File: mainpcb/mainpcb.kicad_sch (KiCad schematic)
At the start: 0 parts

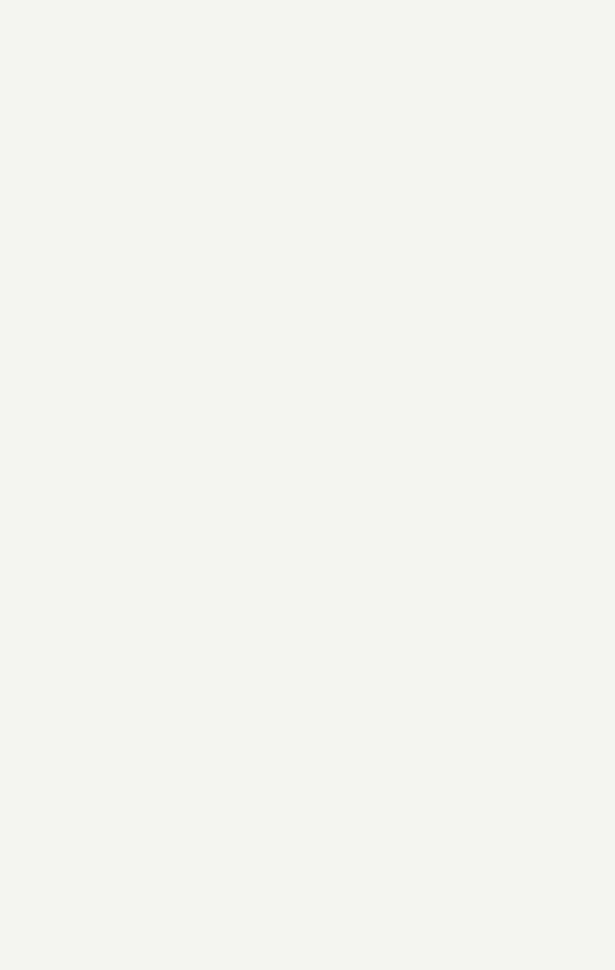
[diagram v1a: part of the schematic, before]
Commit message: Some hand components, PSU changes
Updated PSU to 24V rail regulated to 5V and 3.3V. Hopefully we won't need a 12V rail. Made some part selections, added IO expander for hand, mosfet, made solenoid symbol.
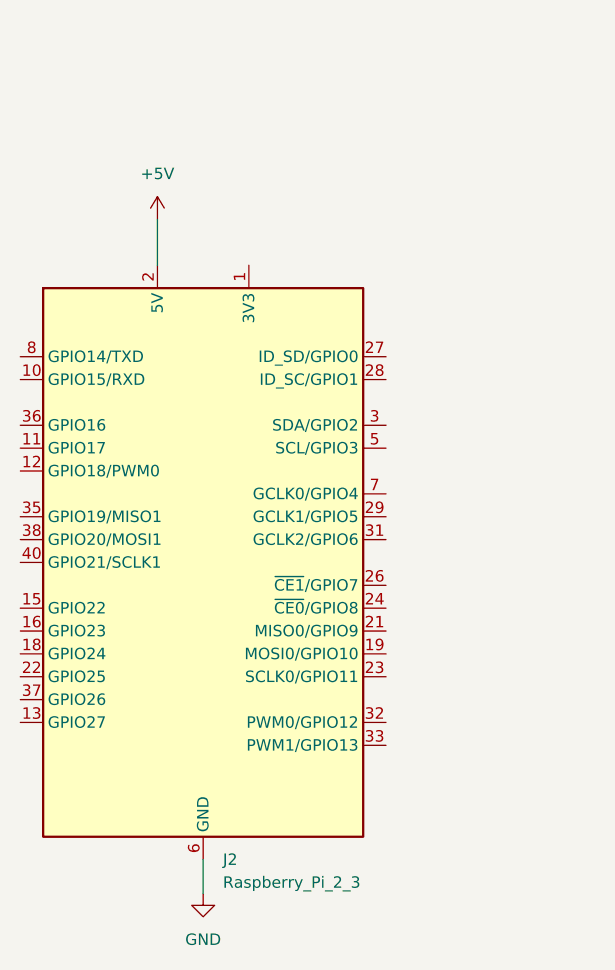
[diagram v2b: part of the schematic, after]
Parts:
- added J2: Raspberry_Pi_2_3, Connector_PinHeader_2.54mm:PinHeader_2x20_P2.54mm_Vertical, symbol Connector:Raspberry_Pi_2_3
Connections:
- new net: J2.1 (3V3), J2.17 (3V3)
- new net +5V: J2.2 (5V), J2.4 (5V)
- new net GND: J2.14 (GND), J2.20 (GND), J2.25 (GND), J2.30 (GND), J2.34 (GND), J2.39 (GND), J2.6 (GND), J2.9 (GND)

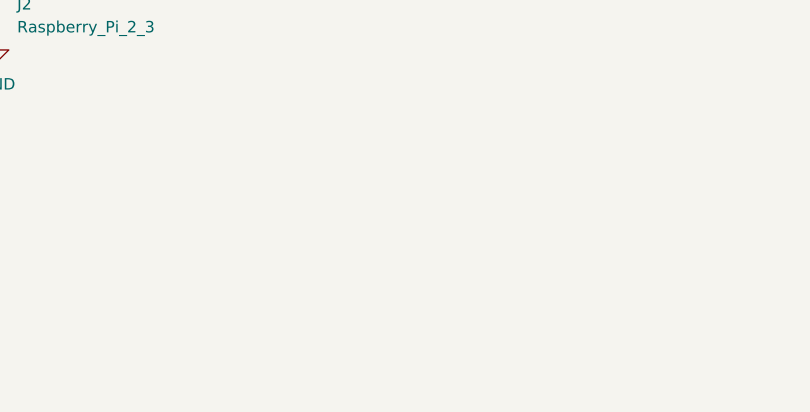
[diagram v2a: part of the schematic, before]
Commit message: Added PCA9615 differential I2C buffer
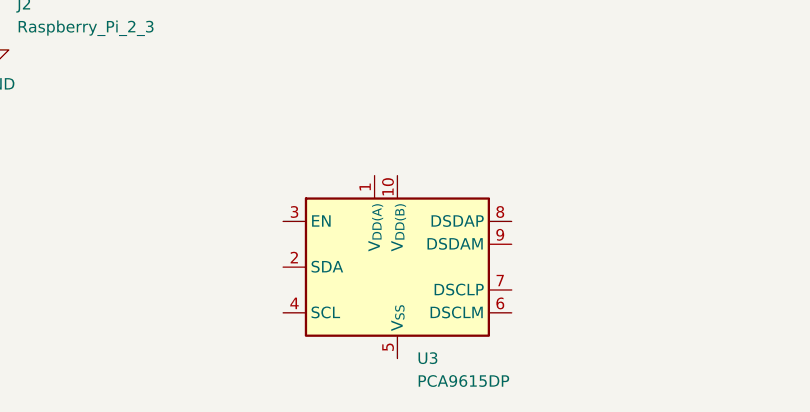
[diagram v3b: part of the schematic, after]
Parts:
- added U3: PCA9615DP, Package_SO:TSSOP-10_3x3mm_P0.5mm, symbol Interface:PCA9615DP
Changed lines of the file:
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@@
+	)
+	(symbol
+		(lib_id "Interface:PCA9615DP")
+		(at 137.16 170.18 0)
+		(unit 1)
+		(exclude_from_sim no)
+		(in_bom yes)
+		(on_board yes)
+		(dnp no)
+		(fields_autoplaced yes)
+		(property "Reference" "U3"
+			(at 139.3541 180.34 0)
+			(effects
+				(font
+					(size 1.27 1.27)
+				)
+				(justify left)
+			)
+		)
+		(property "Value" "PCA9615DP"
+			(at 139.3541 182.88 0)
+			(effects
+				(font
+					(size 1.27 1.27)
+				)
+				(justify left)
+			)
+		)
+		(property "Footprint" "Package_SO:TSSOP-10_3x3mm_P0.5mm"
+			(at 157.48 179.07 0)
+			(effects
+				(font
+					(size 1.27 1.27)
+				)
+				(hide yes)
+			)
+		)
+		(property "Datasheet" "https://www.nxp.com/docs/en/data-sheet/PCA9615.pdf"
+			(at 137.16 181.61 0)
+			(effects
+				(font
+					(size 1.27 1.27)
+				)
+				(hide yes)
+			)
+		)
+		(property "Description" "Dual bidirectional hot-swap multipoint bus buffer, SO-8"
+			(at 137.16 170.18 0)
+			(effects
+				(font
+					(size 1.27 1.27)
+				)
+				(hide yes)
+			)
+		)
+		(property "Digikey" "https://www.digikey.ca/en/products/detail/nxp-usa-inc/PCA9615DPZ/14635231"
+			(at 137.16 170.18 0)
+			(effects
+				(font
+					(size 1.27 1.27)
+				)
+				(hide yes)
+			)
+		)
+		(pin "9"
+		)
+		(pin "2"
+		)
+		(pin "4"
+		)
+		(pin "7"
+		)
+		(pin "10"
+		)
+		(pin "6"
+		)
+		(pin "3"
+		)
+		(pin "5"
+		)
+		(pin "1"
+		)
+		(pin "8"
+		)
+		(instances
+			(project "mainpcb"
+				(path "/8e899647-a0f4-47d2-9d4a-2e9de2221eca"
+					(reference "U3")
+					(unit 1)
+				)
+			)
+		)
 	)
 	(symbol

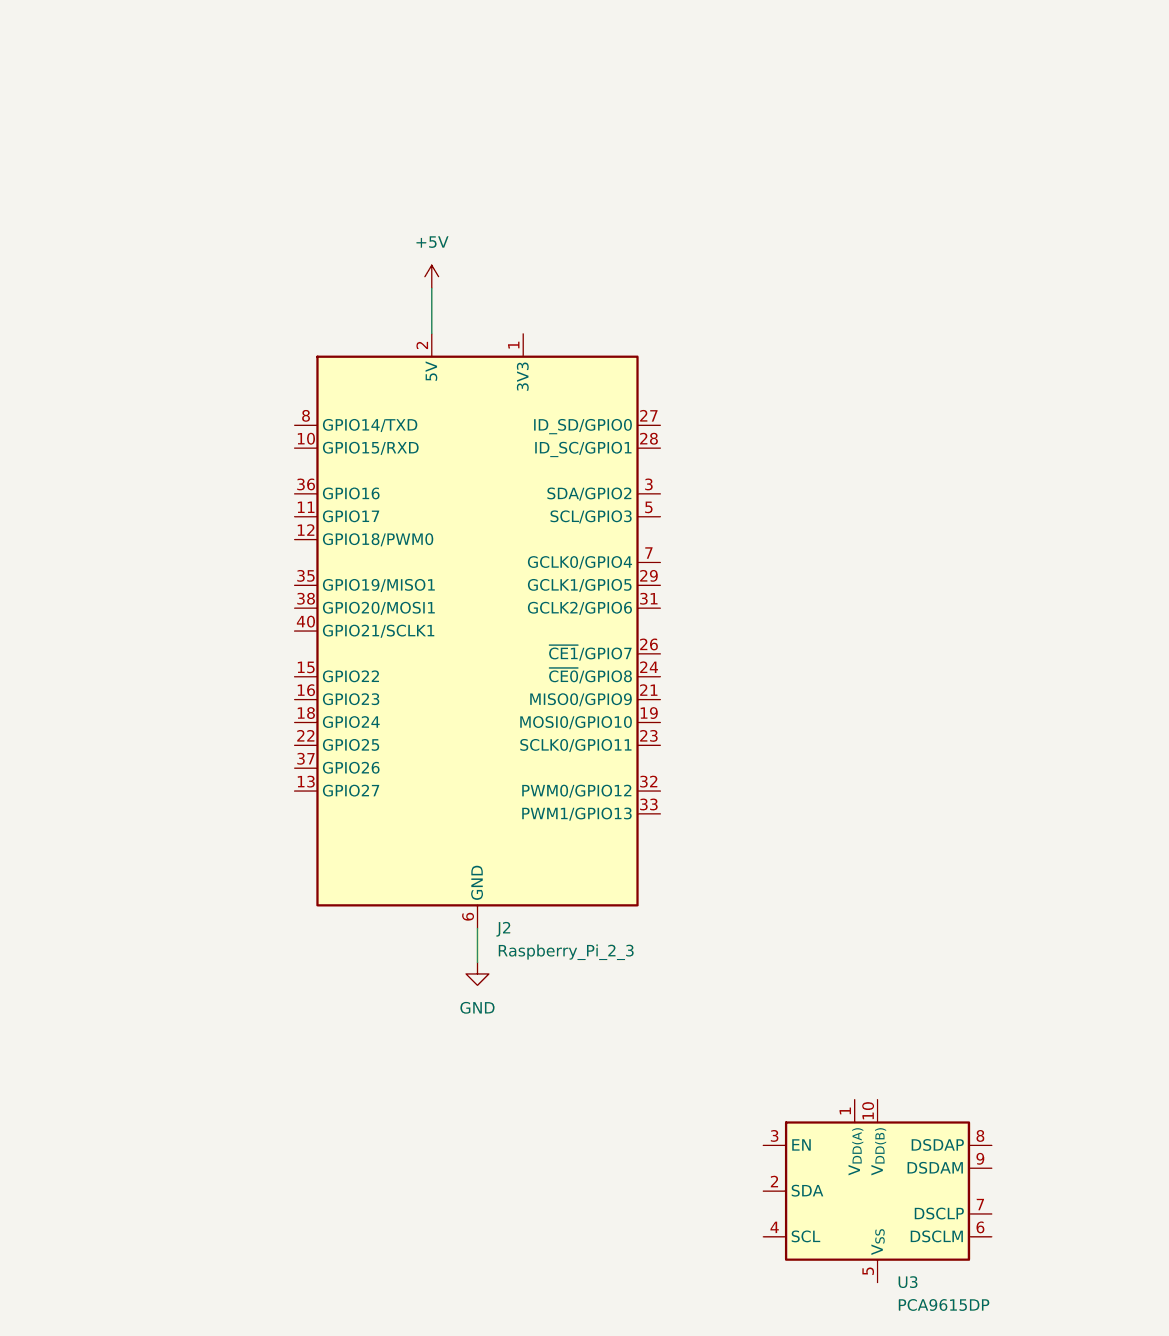
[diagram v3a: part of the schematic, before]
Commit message: Added 12V power rail and regulator
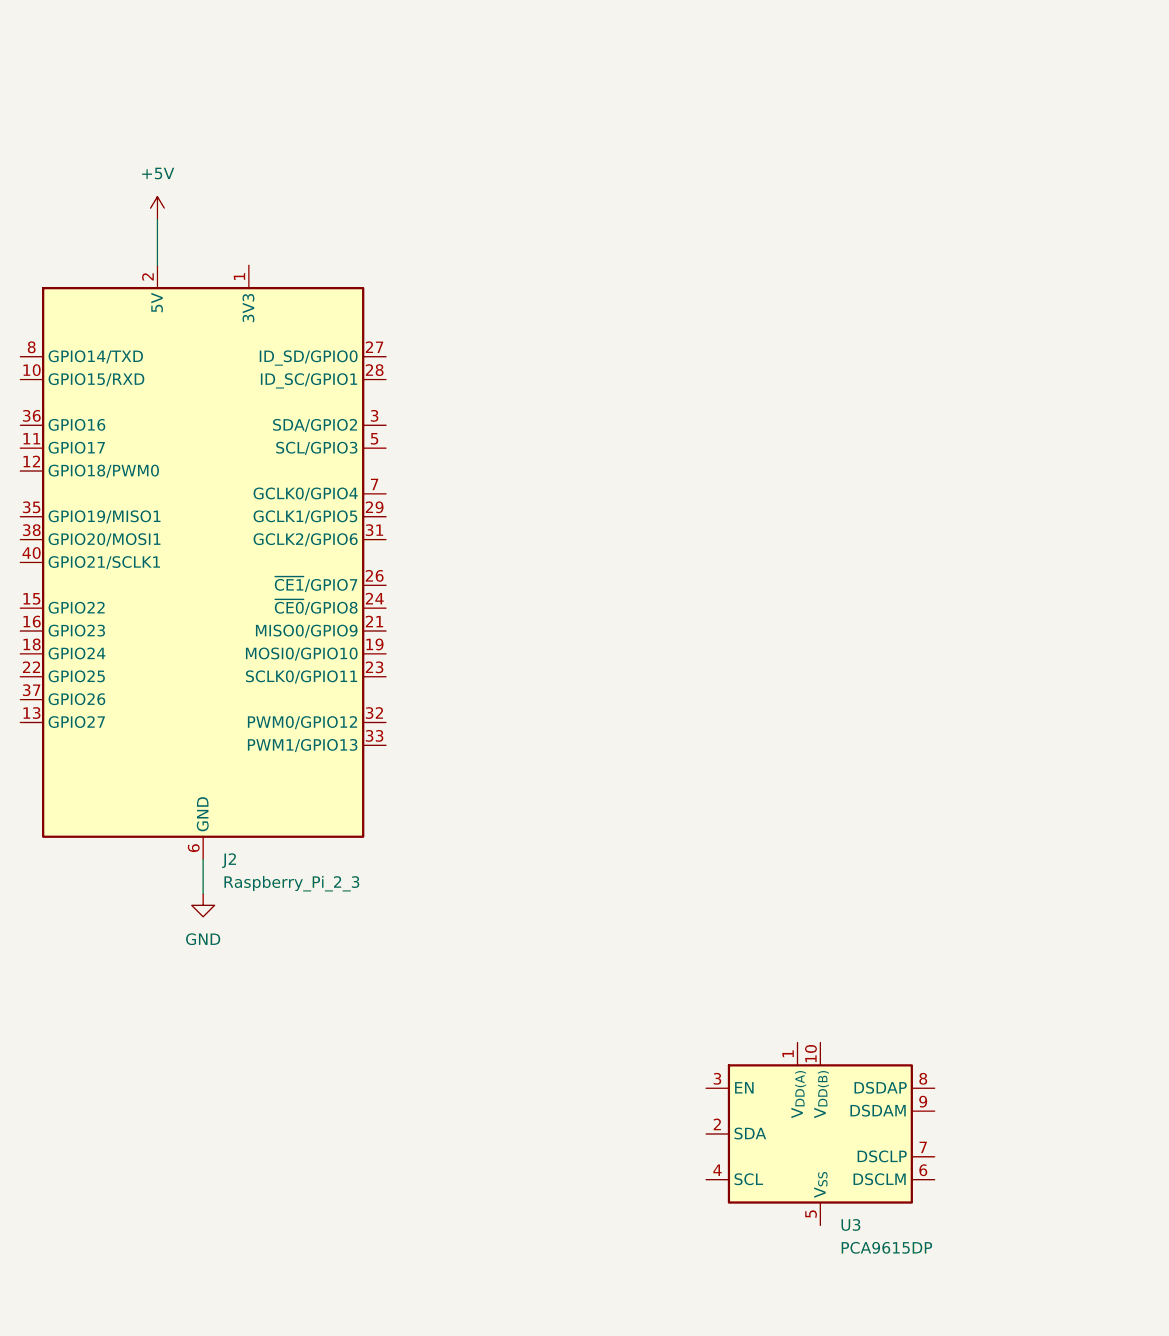
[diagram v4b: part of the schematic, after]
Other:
- moved on the sheet: J2, U3
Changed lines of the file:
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@@
 	(wire
 		(pts
-			(xy 92.71 140.97) (xy 92.71 144.78)
+			(xy 62.23 133.35) (xy 62.23 137.16)
 		)
 		(stroke
@@
 	(wire
 		(pts
-			(xy 87.63 69.85) (xy 87.63 74.93)
+			(xy 57.15 62.23) (xy 57.15 67.31)
 		)
 		(stroke
@@
 	(symbol
 		(lib_id "power:GND")
-		(at 92.71 144.78 0)
+		(at 62.23 137.16 0)
 		(unit 1)
 		(exclude_from_sim no)
@@
 		(fields_autoplaced yes)
 		(property "Reference" "#PWR014"
-			(at 92.71 151.13 0)
+			(at 62.23 143.51 0)
 			(effects
 				(font
@@
 		)
 		(property "Value" "GND"
-			(at 92.71 149.86 0)
+			(at 62.23 142.24 0)
 			(effects
 				(font
@@
 		)
 		(property "Footprint" ""
-			(at 92.71 144.78 0)
+			(at 62.23 137.16 0)
 			(effects
 				(font
@@
 		)
 		(property "Datasheet" ""
-			(at 92.71 144.78 0)
+			(at 62.23 137.16 0)
 			(effects
 				(font
@@
 		)
 		(property "Description" "Power symbol creates a global label with name \"GND\" , ground"
-			(at 92.71 144.78 0)
+			(at 62.23 137.16 0)
 			(effects
 				(font
@@
 	(symbol
 		(lib_id "Connector:Raspberry_Pi_2_3")
-		(at 92.71 107.95 0)
+		(at 62.23 100.33 0)
 		(unit 1)
 		(exclude_from_sim no)
@@
 		(fields_autoplaced yes)
 		(property "Reference" "J2"
-			(at 94.9041 140.97 0)
+			(at 64.4241 133.35 0)
 			(effects
 				(font
@@
 		)
 		(property "Value" "Raspberry_Pi_2_3"
-			(at 94.9041 143.51 0)
+			(at 64.4241 135.89 0)
 			(effects
 				(font
@@
 		)
 		(property "Footprint" "Connector_PinHeader_2.54mm:PinHeader_2x20_P2.54mm_Vertical"
-			(at 92.71 107.95 0)
+			(at 62.23 100.33 0)
 			(effects
 				(font
@@
 		)
 		(property "Datasheet" "https://www.raspberrypi.org/documentation/hardware/raspberrypi/schematics/rpi_SCH_3bplus_1p0_reduced.pdf"
-			(at 153.67 152.4 0)
+			(at 123.19 144.78 0)
 			(effects
 				(font
@@
 		)
 		(property "Description" "expansion header for Raspberry Pi 2 & 3"
-			(at 92.71 107.95 0)
+			(at 62.23 100.33 0)
 			(effects
 				(font
@@
 	(symbol
 		(lib_id "Interface:PCA9615DP")
-		(at 137.16 170.18 0)
+		(at 130.81 163.83 0)
 		(unit 1)
 		(exclude_from_sim no)
@@
 		(fields_autoplaced yes)
 		(property "Reference" "U3"
-			(at 139.3541 180.34 0)
+			(at 133.0041 173.99 0)
 			(effects
 				(font
@@
 		)
 		(property "Value" "PCA9615DP"
-			(at 139.3541 182.88 0)
+			(at 133.0041 176.53 0)
 			(effects
 				(font
@@
 		)
 		(property "Footprint" "Package_SO:TSSOP-10_3x3mm_P0.5mm"
-			(at 157.48 179.07 0)
+			(at 151.13 172.72 0)
 			(effects
 				(font
@@
 		)
 		(property "Datasheet" "https://www.nxp.com/docs/en/data-sheet/PCA9615.pdf"
-			(at 137.16 181.61 0)
+			(at 130.81 175.26 0)
 			(effects
 				(font
@@
 		)
 		(property "Description" "Dual bidirectional hot-swap multipoint bus buffer, SO-8"
-			(at 137.16 170.18 0)
+			(at 130.81 163.83 0)
 			(effects
 				(font
@@
 		)
 		(property "Digikey" "https://www.digikey.ca/en/products/detail/nxp-usa-inc/PCA9615DPZ/14635231"
-			(at 137.16 170.18 0)
+			(at 130.81 163.83 0)
 			(effects
 				(font
@@
 	(symbol
 		(lib_id "power:+5V")
-		(at 87.63 69.85 0)
+		(at 57.15 62.23 0)
 		(unit 1)
 		(exclude_from_sim no)
@@
 		(fields_autoplaced yes)
 		(property "Reference" "#PWR013"
-			(at 87.63 73.66 0)
+			(at 57.15 66.04 0)
 			(effects
 				(font
@@
 		)
 		(property "Value" "+5V"
-			(at 87.63 64.77 0)
+			(at 57.15 57.15 0)
 			(effects
 				(font
@@
 		)
 		(property "Footprint" ""
-			(at 87.63 69.85 0)
+			(at 57.15 62.23 0)
 			(effects
 				(font
@@
 		)
 		(property "Datasheet" ""
-			(at 87.63 69.85 0)
+			(at 57.15 62.23 0)
 			(effects
 				(font
@@
 		)
 		(property "Description" "Power symbol creates a global label with name \"+5V\""
-			(at 87.63 69.85 0)
-			(effects
-				(font
+			(at 57.15 62.23 0)
+			(effects
+				(font

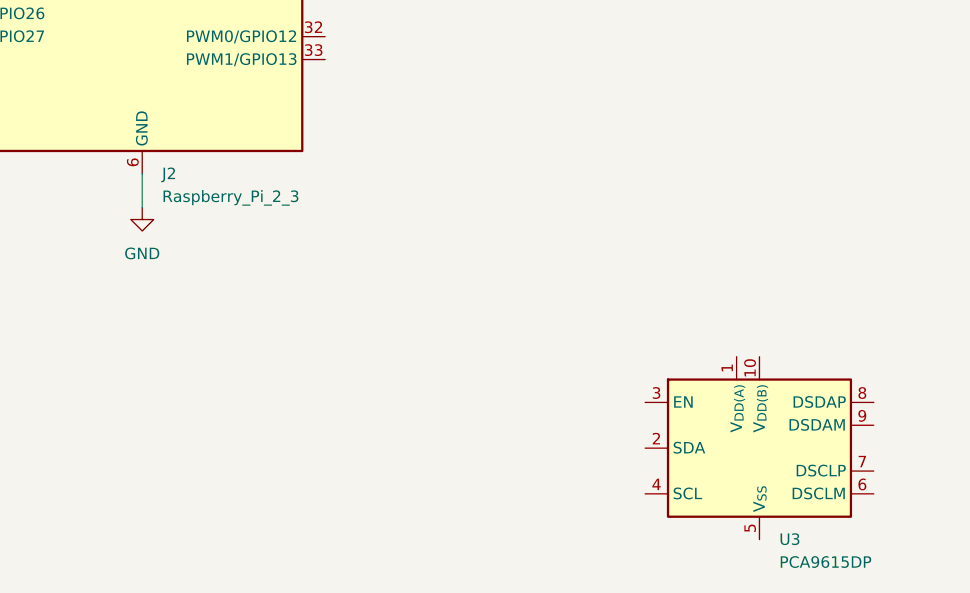
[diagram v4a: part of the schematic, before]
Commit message: Created LM2678 12V regulator symbol
Updated 12V regulator circuit
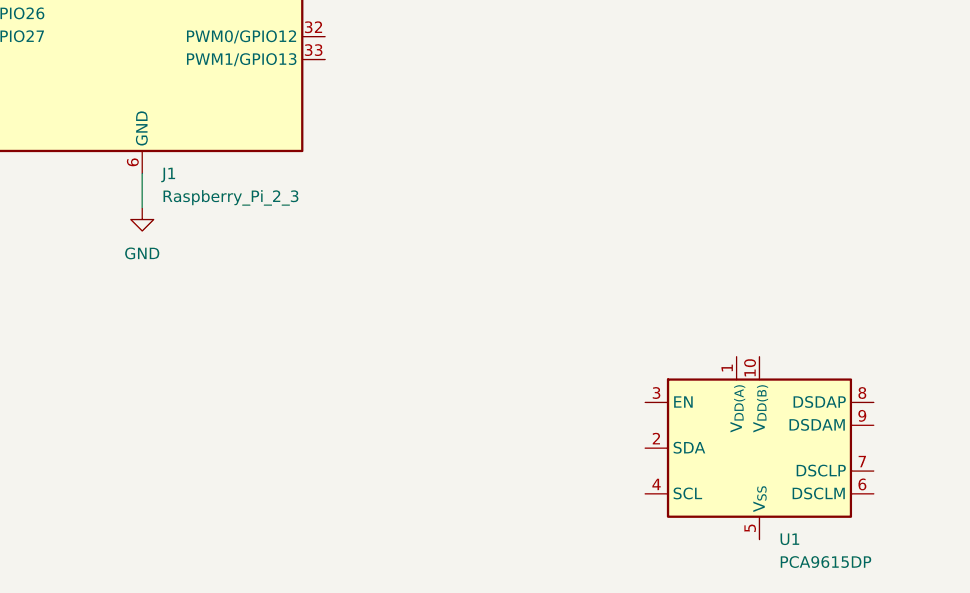
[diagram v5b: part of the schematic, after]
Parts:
- renumbered J2 to J1, U3 to U1
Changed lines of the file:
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@@
 		(dnp no)
 		(fields_autoplaced yes)
-		(property "Reference" "#PWR014"
+		(property "Reference" "#PWR02"
 			(at 62.23 143.51 0)
 			(effects
@@
 			(project ""
 				(path "/8e899647-a0f4-47d2-9d4a-2e9de2221eca"
-					(reference "#PWR014")
+					(reference "#PWR02")
 					(unit 1)
 				)
@@
 		(dnp no)
 		(fields_autoplaced yes)
-		(property "Reference" "J2"
+		(property "Reference" "J1"
 			(at 64.4241 133.35 0)
 			(effects
@@
 			(project ""
 				(path "/8e899647-a0f4-47d2-9d4a-2e9de2221eca"
-					(reference "J2")
+					(reference "J1")
 					(unit 1)
 				)
@@
 		(dnp no)
 		(fields_autoplaced yes)
-		(property "Reference" "U3"
+		(property "Reference" "U1"
 			(at 133.0041 173.99 0)
 			(effects
@@
 			(project "mainpcb"
 				(path "/8e899647-a0f4-47d2-9d4a-2e9de2221eca"
-					(reference "U3")
+					(reference "U1")
 					(unit 1)
 				)
@@
 		(dnp no)
 		(fields_autoplaced yes)
-		(property "Reference" "#PWR013"
+		(property "Reference" "#PWR01"
 			(at 57.15 66.04 0)
 			(effects
@@
 			(project ""
 				(path "/8e899647-a0f4-47d2-9d4a-2e9de2221eca"
-					(reference "#PWR013")
+					(reference "#PWR01")
 					(unit 1)
 				)
